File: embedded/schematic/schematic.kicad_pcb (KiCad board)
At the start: 12 copper layers, 71.1 x 30.5 mm, 10 parts

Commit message: Updated schematics
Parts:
- removed the REF** at (61.9, 47.3)
- removed the REF** at (86.4, 35.6)
- removed the REF** at (86.4, 45.7)
- removed the REF** at (53.3, 38.1)
- removed the REF** at (50.8, 38.1)
- removed the REF** at (55.9, 38.1)
- removed the REF** at (38.1, 45.7)
- removed the REF** at (24.7, 43.2)
- added BAT: PinHeader_1x02_P2.54mm_Horizontal, Connector_PinHeader_2.54mm:PinHeader_1x02_P2.54mm_Horizontal, F.Cu at (27.9, 55.9)
- added BuckBoost3.3V1: ~, custom:BuckBoost3.3V, F.Cu at (68.6, 45.7)
- added HUM: PinHeader_1x03_P2.54mm_Horizontal, Connector_PinHeader_2.54mm:PinHeader_1x03_P2.54mm_Horizontal, F.Cu at (27.9, 48.3)
- added Q1: AO3400A, Package_TO_SOT_SMD:SOT-23, F.Cu at (34.6, 48.3)
- added R1: 1M, Resistor_THT:R_Axial_DIN0207_L6.3mm_D2.5mm_P10.16mm_Horizontal, F.Cu at (38.1, 50.8)
- added R2: 1M, Resistor_THT:R_Axial_DIN0207_L6.3mm_D2.5mm_P10.16mm_Horizontal, F.Cu at (48.3, 48.3)
- added R3: 4.7k, Resistor_THT:R_Axial_DIN0207_L6.3mm_D2.5mm_P10.16mm_Horizontal, F.Cu at (45.7, 40.6)
- added TMP: PinHeader_1x03_P2.54mm_Horizontal, Connector_PinHeader_2.54mm:PinHeader_1x03_P2.54mm_Horizontal, F.Cu at (27.9, 38.1)
- moved REF** 28.4 mm to (40.6, 30.5)
- moved REF** 28.4 mm to (40.6, 55.9)
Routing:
- net (no net): track 330.1 -> 0.00 mm
- net GND: track 0.00 -> 109.3 mm
- net BAT+: track 0.00 -> 51.0 mm
- net SEN: track 0.00 -> 49.7 mm
- net HUM: track 0.00 -> 44.4 mm
- net 3.3V: track 0.00 -> 41.9 mm
- net TMP: track 0.00 -> 39.3 mm
- net BAT: track 0.00 -> 26.6 mm
- net Net-(Q1-D): track 0.00 -> 2.54 mm
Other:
- board size 71.1 x 30.5 mm -> 55.9 x 38.1 mm
- copper layers 12 -> 2
- board text removed: "+"
- board text removed: "-"
- board text removed: "A"
- board text removed: "BAT"
- board text removed: "BoostBuck"
- board text removed: "HUM"
- board text removed: "R1_1"
- board text removed: "R1_2"
- board text removed: "R2"
- board text removed: "TMP"

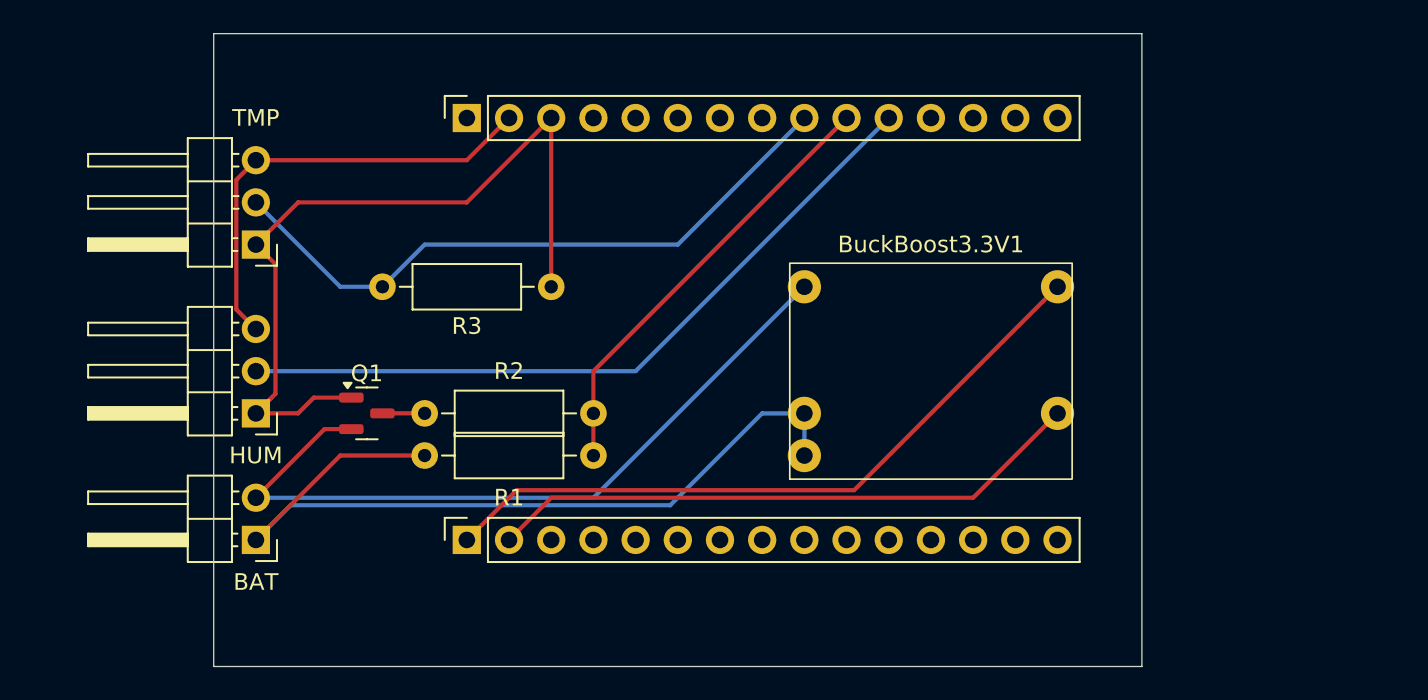
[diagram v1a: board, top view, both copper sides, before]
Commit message: Added compact schematic
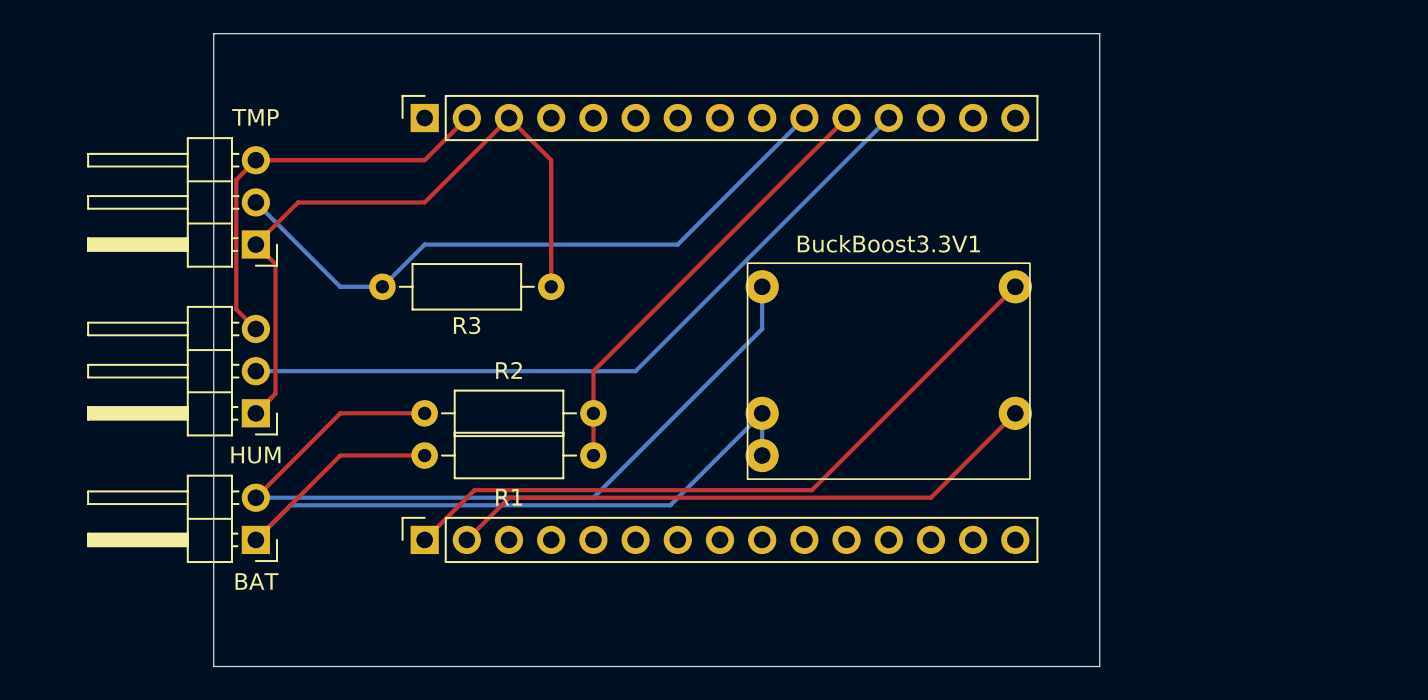
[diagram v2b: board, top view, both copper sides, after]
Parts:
- removed Q1: AO3400A, Package_TO_SOT_SMD:SOT-23
- moved REF** 2.54 mm to (38.1, 30.5)
- moved REF** 2.54 mm to (38.1, 55.9)
- moved BuckBoost3.3V1 2.54 mm to (66.0, 45.7)
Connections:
- R2 pad 2: Net-(Q1-D) -> GND
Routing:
- net SEN: track 49.7 -> 42.1 mm
- net Net-(Q1-D): track 2.54 -> 0.00 mm
- net BAT+: track 51.0 -> 48.4 mm
- net GND: track 109.3 -> 110.6 mm
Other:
- board size 55.9 x 38.1 mm -> 53.3 x 38.1 mm

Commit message: updated compact schematic
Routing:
- net HUM: track 44.4 -> 41.9 mm
- net TMP: track 39.3 -> 36.8 mm
- net BAT: track 26.6 -> 25.6 mm
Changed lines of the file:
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@@
 	)
 	(segment
-		(start 48.26 45.72)
-		(end 63.5 30.48)
+		(start 60.96 30.48)
+		(end 48.26 43.18)
 		(width 0.254)
 		(layer "F.Cu")
@@
 	)
 	(segment
-		(start 48.26 48.26)
-		(end 48.26 45.72)
+		(start 48.26 43.18)
+		(end 48.26 48.26)
 		(width 0.254)
 		(layer "F.Cu")
@@
 	)
 	(segment
-		(start 53.34 38.1)
-		(end 38.1 38.1)
+		(start 38.1 38.1)
+		(end 50.8 38.1)
 		(width 0.254)
 		(layer "B.Cu")
@@
 	)
 	(segment
-		(start 60.96 30.48)
-		(end 53.34 38.1)
+		(start 50.8 38.1)
+		(end 58.42 30.48)
 		(width 0.254)
 		(layer "B.Cu")
@@
 	)
 	(segment
-		(start 66.04 30.48)
-		(end 50.8 45.72)
+		(start 48.26 45.72)
+		(end 63.5 30.48)
 		(width 0.254)
 		(layer "B.Cu")
@@
 	)
 	(segment
-		(start 50.8 45.72)
-		(end 27.94 45.72)
+		(start 27.94 45.72)
+		(end 48.26 45.72)
 		(width 0.254)
 		(layer "B.Cu")
